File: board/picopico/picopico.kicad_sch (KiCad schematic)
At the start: 45 parts, among them J2 display, J3 USB_B_Micro, Q1 BC817, Q2 BC817, SW1 SW_SPDT, SW3 SW_Push, SW5 SW_Push, SW6 SW_Push, SW7 SW_Push, SW8 SW_Push, U1 ESP32-WROVER-E, U2 volume_wheel, U3 AMS1117-3.3, U4 audio, U5 STC4054GR, U6 CH340C

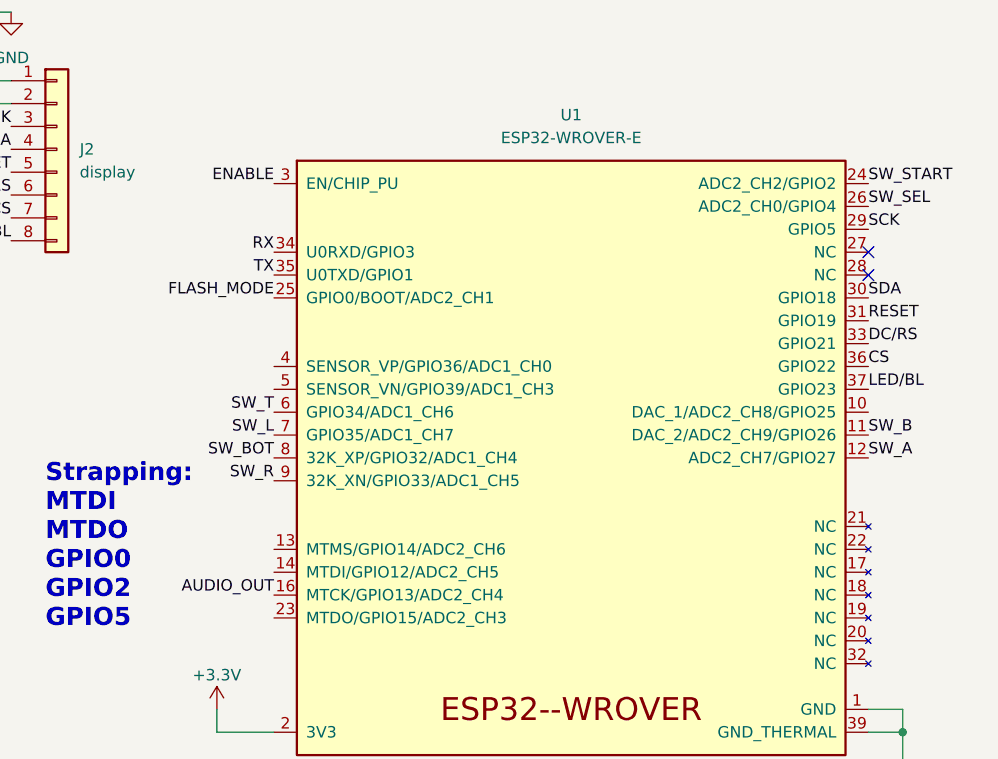
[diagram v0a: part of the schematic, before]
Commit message: move esp down
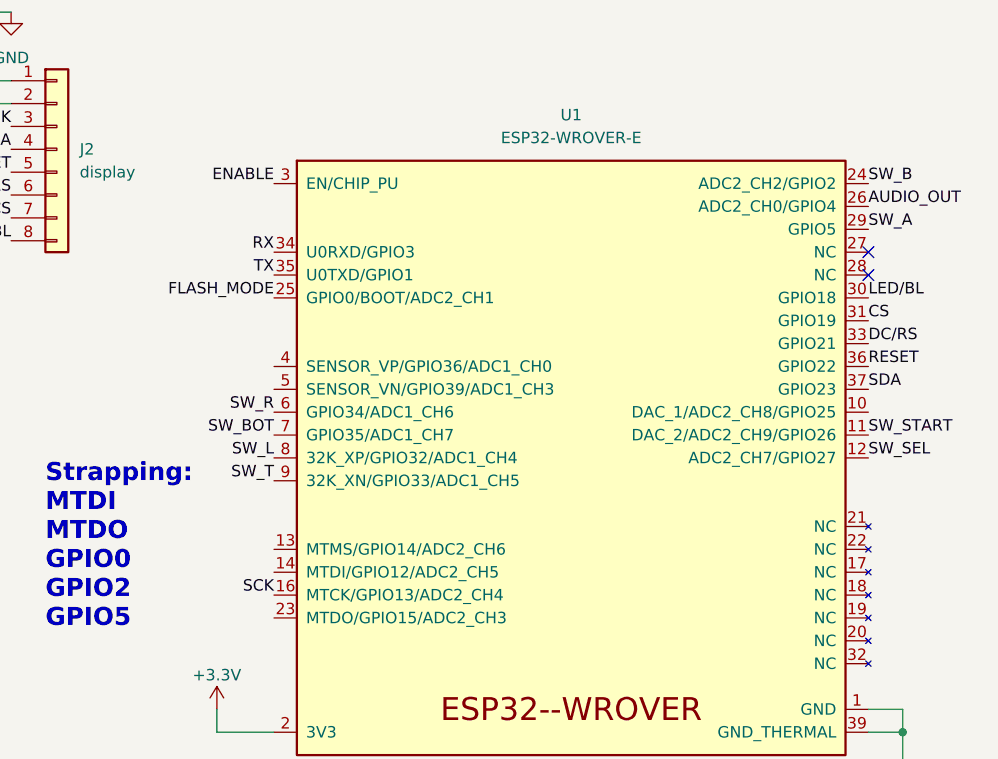
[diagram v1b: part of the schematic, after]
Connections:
- net AUDIO_OUT: now also U1.26 (ADC2_CH0/GPIO4); no longer U1.16 (MTCK/GPIO13/ADC2_CH4)
- net CS: now also U1.31 (GPIO19); no longer U1.36 (GPIO22)
- net LED/BL: now also U1.30 (GPIO18); no longer U1.37 (GPIO23)
- net RESET: now also U1.36 (GPIO22); no longer U1.31 (GPIO19)
- net SCK: now also U1.16 (MTCK/GPIO13/ADC2_CH4); no longer U1.29 (GPIO5)
- net SDA: now also U1.37 (GPIO23); no longer U1.30 (GPIO18)
- net SW_A: now also U1.29 (GPIO5); no longer U1.12 (ADC2_CH7/GPIO27)
- net SW_B: now also U1.24 (ADC2_CH2/GPIO2); no longer U1.11 (DAC_2/ADC2_CH9/GPIO26)
- net SW_BOT: now also U1.7 (GPIO35/ADC1_CH7); no longer U1.8 (32K_XP/GPIO32/ADC1_CH4)
- net SW_L: now also U1.8 (32K_XP/GPIO32/ADC1_CH4); no longer U1.7 (GPIO35/ADC1_CH7)
- net SW_R: now also U1.6 (GPIO34/ADC1_CH6); no longer U1.9 (32K_XN/GPIO33/ADC1_CH5)
- net SW_SEL: now also U1.12 (ADC2_CH7/GPIO27); no longer U1.26 (ADC2_CH0/GPIO4)
- net SW_START: now also U1.11 (DAC_2/ADC2_CH9/GPIO26); no longer U1.24 (ADC2_CH2/GPIO2)
- net SW_T: now also U1.9 (32K_XN/GPIO33/ADC1_CH5); no longer U1.6 (GPIO34/ADC1_CH6)
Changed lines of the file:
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@@
     (effects (font (size 2 2) (thickness 0.4) bold) (justify left bottom))
-  )
-  (label "SCK" (at 273.05 43.18 0)
-    (effects (font (size 1.27 1.27)) (justify left bottom))
   )
   (label "RX" (at 129.54 73.66 0)
     (effects (font (size 1.27 1.27)) (justify left bottom))
   )
-  (label "SW_A" (at 104.14 129.54 180)
-    (effects (font (size 1.27 1.27)) (justify right bottom))
-  )
-  (label "SDA" (at 273.05 50.8 0)
+  (label "SW_START" (at 273.05 66.04 0)
     (effects (font (size 1.27 1.27)) (justify left bottom))
   )
-  (label "SW_L" (at 207.01 66.04 180)
+  (label "SW_A" (at 104.14 129.54 180)
     (effects (font (size 1.27 1.27)) (justify right bottom))
   )
@@
     (effects (font (size 1.27 1.27)) (justify left bottom))
   )
-  (label "SW_A" (at 273.05 68.58 0)
-    (effects (font (size 1.27 1.27)) (justify left bottom))
-  )
-  (label "LED{slash}BL" (at 273.05 60.96 0)
-    (effects (font (size 1.27 1.27)) (justify left bottom))
-  )
-  (label "SW_SEL" (at 273.05 40.64 0)
+  (label "RESET" (at 273.05 58.42 0)
     (effects (font (size 1.27 1.27)) (justify left bottom))
   )
@@
     (effects (font (size 1.27 1.27)) (justify left bottom))
   )
-  (label "SW_START" (at 273.05 38.1 0)
-    (effects (font (size 1.27 1.27)) (justify left bottom))
-  )
-  (label "RESET" (at 273.05 53.34 0)
+  (label "SW_A" (at 273.05 43.18 0)
     (effects (font (size 1.27 1.27)) (justify left bottom))
   )
@@
     (effects (font (size 1.27 1.27)) (justify right bottom))
   )
-  (label "SW_BOT" (at 207.01 68.58 180)
-    (effects (font (size 1.27 1.27)) (justify right bottom))
-  )
   (label "AUDIO_OUT" (at 209.55 130.81 180)
     (effects (font (size 1.27 1.27)) (justify right bottom))
@@
   (label "USB_VIN" (at 64.77 41.91 0)
     (effects (font (size 1.27 1.27)) (justify left bottom))
+  )
+  (label "SW_T" (at 207.01 71.12 180)
+    (effects (font (size 1.27 1.27)) (justify right bottom))
   )
   (label "DC{slash}RS" (at 273.05 55.88 0)
@@
     (effects (font (size 1.27 1.27)) (justify right bottom))
   )
+  (label "SCK" (at 207.01 83.82 180)
+    (effects (font (size 1.27 1.27)) (justify right bottom))
+  )
+  (label "SW_SEL" (at 273.05 68.58 0)
+    (effects (font (size 1.27 1.27)) (justify left bottom))
+  )
   (label "ENABLE" (at 207.01 38.1 180)
     (effects (font (size 1.27 1.27)) (justify right bottom))
@@
     (effects (font (size 1.27 1.27)) (justify right bottom))
   )
-  (label "SW_T" (at 207.01 63.5 180)
+  (label "FLASH_MODE" (at 207.01 50.8 180)
     (effects (font (size 1.27 1.27)) (justify right bottom))
   )
-  (label "CS" (at 273.05 58.42 0)
+  (label "CS" (at 273.05 53.34 0)
     (effects (font (size 1.27 1.27)) (justify left bottom))
-  )
-  (label "FLASH_MODE" (at 207.01 50.8 180)
-    (effects (font (size 1.27 1.27)) (justify right bottom))
   )
   (label "TX" (at 104.14 76.2 0)
@@
     (effects (font (size 1.27 1.27)) (justify right bottom))
   )
+  (label "AUDIO_OUT" (at 273.05 40.64 0)
+    (effects (font (size 1.27 1.27)) (justify left bottom))
+  )
   (label "SW_L" (at 62.23 129.54 0)
     (effects (font (size 1.27 1.27)) (justify left bottom))
@@
     (effects (font (size 1.27 1.27)) (justify right bottom))
   )
+  (label "SW_L" (at 207.01 68.58 180)
+    (effects (font (size 1.27 1.27)) (justify right bottom))
+  )
   (label "UD-" (at 77.47 40.64 180)
     (effects (font (size 1.27 1.27)) (justify right bottom))
   )
-  (label "SW_R" (at 207.01 71.12 180)
-    (effects (font (size 1.27 1.27)) (justify right bottom))
+  (label "LED{slash}BL" (at 273.05 50.8 0)
+    (effects (font (size 1.27 1.27)) (justify left bottom))
+  )
+  (label "SDA" (at 273.05 60.96 0)
+    (effects (font (size 1.27 1.27)) (justify left bottom))
   )
   (label "SW_B" (at 104.14 139.7 180)
@@
     (effects (font (size 1.27 1.27)) (justify right bottom))
   )
+  (label "SW_R" (at 207.01 63.5 180)
+    (effects (font (size 1.27 1.27)) (justify right bottom))
+  )
   (label "ENABLE" (at 134.62 77.47 0)
     (effects (font (size 1.27 1.27)) (justify left bottom))
@@
     (effects (font (size 1.27 1.27)) (justify right bottom))
   )
-  (label "SW_B" (at 273.05 66.04 0)
+  (label "SW_BOT" (at 207.01 66.04 180)
+    (effects (font (size 1.27 1.27)) (justify right bottom))
+  )
+  (label "SW_B" (at 273.05 38.1 0)
     (effects (font (size 1.27 1.27)) (justify left bottom))
   )
-  (label "AUDIO_OUT" (at 207.01 83.82 180)
-    (effects (font (size 1.27 1.27)) (justify right bottom))
-  )
   (symbol (lib_id "Switch:SW_Push") (at 90.17 139.7 0) (unit 1)

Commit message: more board changes
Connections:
- net SW_A: now also U1.24 (ADC2_CH2/GPIO2); no longer U1.29 (GPIO5)
- net SW_B: now also U1.29 (GPIO5); no longer U1.24 (ADC2_CH2/GPIO2)
- net SW_BOT: now also U1.10 (DAC_1/ADC2_CH8/GPIO25); no longer U1.7 (GPIO35/ADC1_CH7)
- net SW_L: now also U1.11 (DAC_2/ADC2_CH9/GPIO26); no longer U1.8 (32K_XP/GPIO32/ADC1_CH4)
- net SW_R: now also U1.9 (32K_XN/GPIO33/ADC1_CH5); no longer U1.6 (GPIO34/ADC1_CH6)
- net SW_SEL: now also U1.7 (GPIO35/ADC1_CH7); no longer U1.12 (ADC2_CH7/GPIO27)
- net SW_START: now also U1.6 (GPIO34/ADC1_CH6); no longer U1.11 (DAC_2/ADC2_CH9/GPIO26)
- net SW_T: now also U1.8 (32K_XP/GPIO32/ADC1_CH4); no longer U1.9 (32K_XN/GPIO33/ADC1_CH5)
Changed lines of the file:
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@@
-    (effects (font (size 1.27 1.27)) (justify left bottom))
-  )
-  (label "SW_START" (at 273.05 66.04 0)
     (effects (font (size 1.27 1.27)) (justify left bottom))
   )
   (label "SW_A" (at 104.14 129.54 180)
     (effects (font (size 1.27 1.27)) (justify right bottom))
+  )
+  (label "SW_T" (at 207.01 68.58 180)
+    (effects (font (size 1.27 1.27)) (justify right bottom))
+  )
+  (label "SW_BOT" (at 273.05 63.5 0)
+    (effects (font (size 1.27 1.27)) (justify left bottom))
   )
   (label "DC{slash}RS" (at 177.8 39.37 180)
@@
   )
   (label "RESET" (at 273.05 58.42 0)
+    (effects (font (size 1.27 1.27)) (justify left bottom))
+  )
+  (label "SW_B" (at 273.05 43.18 0)
     (effects (font (size 1.27 1.27)) (justify left bottom))
   )
@@
     (effects (font (size 1.27 1.27)) (justify left bottom))
   )
-  (label "SW_A" (at 273.05 43.18 0)
-    (effects (font (size 1.27 1.27)) (justify left bottom))
-  )
   (label "RX" (at 207.01 45.72 180)
     (effects (font (size 1.27 1.27)) (justify right bottom))
@@
     (effects (font (size 1.27 1.27)) (justify left bottom))
   )
-  (label "SW_T" (at 207.01 71.12 180)
+  (label "SW_START" (at 207.01 63.5 180)
     (effects (font (size 1.27 1.27)) (justify right bottom))
   )
@@
     (effects (font (size 1.27 1.27)) (justify right bottom))
   )
-  (label "SW_SEL" (at 273.05 68.58 0)
-    (effects (font (size 1.27 1.27)) (justify left bottom))
-  )
   (label "ENABLE" (at 207.01 38.1 180)
     (effects (font (size 1.27 1.27)) (justify right bottom))
+  )
+  (label "SW_L" (at 273.05 66.04 0)
+    (effects (font (size 1.27 1.27)) (justify left bottom))
   )
   (label "UD-" (at 83.82 86.36 180)
@@
     (effects (font (size 1.27 1.27)) (justify right bottom))
   )
+  (label "SW_A" (at 273.05 38.1 0)
+    (effects (font (size 1.27 1.27)) (justify left bottom))
+  )
   (label "FLASH_MODE" (at 207.01 50.8 180)
     (effects (font (size 1.27 1.27)) (justify right bottom))
@@
     (effects (font (size 1.27 1.27)) (justify left bottom))
   )
+  (label "SW_R" (at 207.01 71.12 180)
+    (effects (font (size 1.27 1.27)) (justify right bottom))
+  )
   (label "TX" (at 104.14 76.2 0)
     (effects (font (size 1.27 1.27)) (justify left bottom))
+  )
+  (label "SW_SEL" (at 207.01 66.04 180)
+    (effects (font (size 1.27 1.27)) (justify right bottom))
   )
   (label "SW_SEL" (at 104.14 160.02 180)
@@
     (effects (font (size 1.27 1.27)) (justify right bottom))
   )
-  (label "SW_L" (at 207.01 68.58 180)
-    (effects (font (size 1.27 1.27)) (justify right bottom))
-  )
   (label "UD-" (at 77.47 40.64 180)
     (effects (font (size 1.27 1.27)) (justify right bottom))
@@
     (effects (font (size 1.27 1.27)) (justify right bottom))
   )
-  (label "SW_R" (at 207.01 63.5 180)
-    (effects (font (size 1.27 1.27)) (justify right bottom))
-  )
   (label "ENABLE" (at 134.62 77.47 0)
     (effects (font (size 1.27 1.27)) (justify left bottom))
@@
     (effects (font (size 1.27 1.27)) (justify right bottom))
   )
-  (label "SW_BOT" (at 207.01 66.04 180)
-    (effects (font (size 1.27 1.27)) (justify right bottom))
-  )
-  (label "SW_B" (at 273.05 38.1 0)
-    (effects (font (size 1.27 1.27)) (justify left bottom))
-  )
   (symbol (lib_id "Switch:SW_Push") (at 90.17 139.7 0) (unit 1)

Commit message: more board changes
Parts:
- added TP10, TP4, TP5, TP6, TP7, TP8, TP9: TestPoint, picopico:pad, symbol Connector:TestPoint
- U1: footprint Espressif:ESP32-WROVER-E -> Espressif:ESP32-WROVER-E_ThermalVias
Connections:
- net +3.3V: now also TP4.1, TP7.1
- net ENABLE: now also TP6.1
- net FLASH_MODE: now also TP5.1
- net GND: now also TP10.1, TP8.1
- net USB_VIN: now also TP9.1
